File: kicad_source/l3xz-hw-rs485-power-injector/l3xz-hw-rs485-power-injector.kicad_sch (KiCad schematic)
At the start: 14 parts, among them J1 PowerPole, J2 Conn_01x02, J3 Conn_01x03, J4 SM04B-GHS-TB, J5 EH_S4B-EH, J6 EH_S4B-EH

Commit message: updated pcb
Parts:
- D1: footprint (none) -> LED_SMD:LED_0603_1608Metric
- H1, H2, H3, H4: footprint (none) -> MountingHole:MountingHole_3.2mm_M3_DIN965_Pad; now left out of the parts list
- R1: footprint (none) -> Resistor_SMD:R_0603_1608Metric
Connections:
- no-connect marks 4 -> 5
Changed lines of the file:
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@@
   )
   (no_connect (at 76.2 194.31))
+  (no_connect (at 57.15 109.22))
   (no_connect (at 50.8 194.31))
   (no_connect (at 25.4 194.31))
@@
   )
   (symbol (lib_id "Mechanical:MountingHole_Pad") (at 25.4 191.77 0) (unit 1)
-    (in_bom yes) (on_board yes) (fields_autoplaced)
+    (in_bom no) (on_board yes) (fields_autoplaced)
     (property "Reference" "H1" (id 0) (at 27.94 189.2299 0)
       (effects (font (size 1.27 1.27)) (justify left))
@@
       (effects (font (size 1.27 1.27)) (justify left))
     )
-    (property "Footprint" "" (id 2) (at 25.4 191.77 0)
+    (property "Footprint" "MountingHole:MountingHole_3.2mm_M3_DIN965_Pad" (id 2) (at 25.4 191.77 0)
       (effects (font (size 1.27 1.27)) hide)
     )
@@
   )
   (symbol (lib_id "Mechanical:MountingHole_Pad") (at 76.2 191.77 0) (unit 1)
-    (in_bom yes) (on_board yes) (fields_autoplaced)
+    (in_bom no) (on_board yes) (fields_autoplaced)
     (property "Reference" "H3" (id 0) (at 78.74 189.2299 0)
       (effects (font (size 1.27 1.27)) (justify left))
@@
       (effects (font (size 1.27 1.27)) (justify left))
     )
-    (property "Footprint" "" (id 2) (at 76.2 191.77 0)
+    (property "Footprint" "MountingHole:MountingHole_3.2mm_M3_DIN965_Pad" (id 2) (at 76.2 191.77 0)
       (effects (font (size 1.27 1.27)) hide)
     )
@@
   )
   (symbol (lib_id "Mechanical:MountingHole_Pad") (at 101.6 191.77 0) (unit 1)
-    (in_bom yes) (on_board yes) (fields_autoplaced)
+    (in_bom no) (on_board yes) (fields_autoplaced)
     (property "Reference" "H4" (id 0) (at 104.14 189.2299 0)
       (effects (font (size 1.27 1.27)) (justify left))
@@
       (effects (font (size 1.27 1.27)) (justify left))
     )
-    (property "Footprint" "" (id 2) (at 101.6 191.77 0)
+    (property "Footprint" "MountingHole:MountingHole_3.2mm_M3_DIN965_Pad" (id 2) (at 101.6 191.77 0)
       (effects (font (size 1.27 1.27)) hide)
     )
@@
     (property "Reference" "D1" (id 0) (at 118.0465 60.96 0))
     (property "Value" "LED green" (id 1) (at 118.0465 63.5 0))
-    (property "Footprint" "" (id 2) (at 118.11 67.31 90)
+    (property "Footprint" "LED_SMD:LED_0603_1608Metric" (id 2) (at 118.11 67.31 90)
       (effects (font (size 1.27 1.27)) hide)
     )
@@
   )
   (symbol (lib_id "Mechanical:MountingHole_Pad") (at 50.8 191.77 0) (unit 1)
-    (in_bom yes) (on_board yes) (fields_autoplaced)
+    (in_bom no) (on_board yes) (fields_autoplaced)
     (property "Reference" "H2" (id 0) (at 53.34 189.2299 0)
       (effects (font (size 1.27 1.27)) (justify left))
@@
       (effects (font (size 1.27 1.27)) (justify left))
     )
-    (property "Footprint" "" (id 2) (at 50.8 191.77 0)
+    (property "Footprint" "MountingHole:MountingHole_3.2mm_M3_DIN965_Pad" (id 2) (at 50.8 191.77 0)
       (effects (font (size 1.27 1.27)) hide)
     )
@@
     (property "Reference" "R1" (id 0) (at 107.95 60.96 90))
     (property "Value" "10k" (id 1) (at 107.95 63.5 90))
-    (property "Footprint" "" (id 2) (at 107.95 67.31 0)
+    (property "Footprint" "Resistor_SMD:R_0603_1608Metric" (id 2) (at 107.95 67.31 0)
       (effects (font (size 1.27 1.27)) hide)
     )
@@
     )
     (path "/a191106d-6f54-4859-9ae7-7e90c19ff902"
-      (reference "D1") (unit 1) (value "LED green") (footprint "")
+      (reference "D1") (unit 1) (value "LED green") (footprint "LED_SMD:LED_0603_1608Metric")
     )
     (path "/0f7a0782-5c93-425e-9bb2-af249e5413b1"
-      (reference "H1") (unit 1) (value "MountingHole_Pad") (footprint "")
+      (reference "H1") (unit 1) (value "MountingHole_Pad") (footprint "MountingHole:MountingHole_3.2mm_M3_DIN965_Pad")
     )
     (path "/a24d063b-8999-4513-be31-467144dda607"
-      (reference "H2") (unit 1) (value "MountingHole_Pad") (footprint "")
+      (reference "H2") (unit 1) (value "MountingHole_Pad") (footprint "MountingHole:MountingHole_3.2mm_M3_DIN965_Pad")
     )
     (path "/1a89f90c-ae34-4a19-bdb2-498363cb9261"
-      (reference "H3") (unit 1) (value "MountingHole_Pad") (footprint "")
+      (reference "H3") (unit 1) (value "MountingHole_Pad") (footprint "MountingHole:MountingHole_3.2mm_M3_DIN965_Pad")
     )
     (path "/549e08a5-626b-4ce1-b4f2-0dc3abb4166a"
-      (reference "H4") (unit 1) (value "MountingHole_Pad") (footprint "")
+      (reference "H4") (unit 1) (value "MountingHole_Pad") (footprint "MountingHole:MountingHole_3.2mm_M3_DIN965_Pad")
     )
     (path "/9cff36d3-3837-47cf-8e03-52d1bf5a2a97"
@@
     )
     (path "/d10997a4-c66c-4c0c-b0e2-7abe2be8864b"
-      (reference "R1") (unit 1) (value "10k") (footprint "")
-    )
-  )
+      (reference "R1") (unit 1) (value "10k") (footprint "Resistor_SMD:R_0603_1608Metric")
+    )
+  )

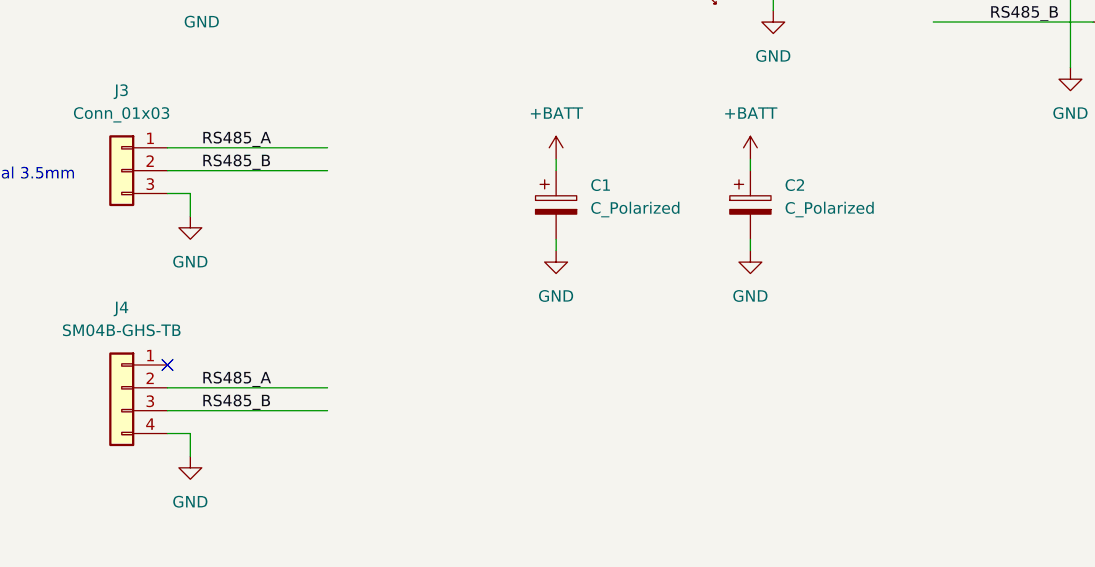
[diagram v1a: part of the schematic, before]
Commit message: added resistor to connect JST GH connector to +BATT
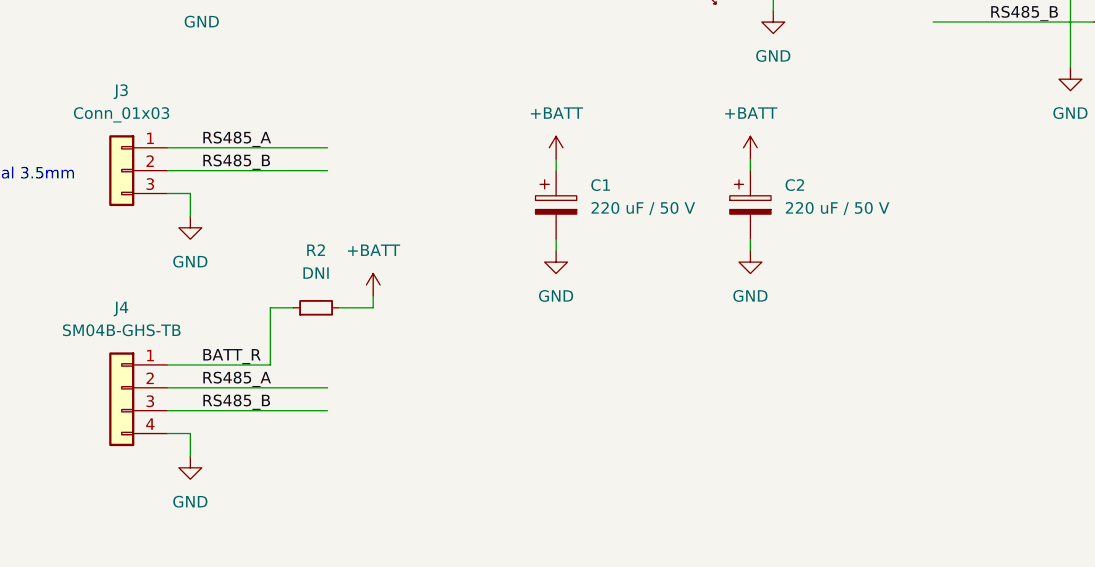
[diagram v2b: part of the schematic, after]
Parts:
- added R2: DNI, Resistor_SMD:R_0603_1608Metric, symbol Device:R_Small
- C1, C2: value C_Polarized -> 220 uF / 50 V
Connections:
- net +BATT: now also R2.2
- net BATT_R: now reaches J4.1 (Pin_1)
- net BATT_R: now also R2.1
- no-connect marks 5 -> 4
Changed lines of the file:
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@@
   (title_block
     (title "l3xz-hw-rs485-power-injector")
-    (date "2023-01-07")
+    (date "2023-01-21")
     (rev "0.1")
     (company "107-systems")
   )
   (no_connect (at 76.2 194.31))
-  (no_connect (at 57.15 109.22))
   (no_connect (at 50.8 194.31))
   (no_connect (at 25.4 194.31))
@@
     (stroke (width 0) (type default) (color 0 0 0 0))
   )
+  (wire (pts (xy 68.58 102.87) (xy 68.58 109.22))
+    (stroke (width 0) (type default) (color 0 0 0 0))
+  )
   (wire (pts (xy 57.15 114.3) (xy 74.93 114.3))
     (stroke (width 0) (type default) (color 0 0 0 0))
   )
+  (wire (pts (xy 71.12 102.87) (xy 68.58 102.87))
+    (stroke (width 0) (type default) (color 0 0 0 0))
+  )
   (wire (pts (xy 60.96 63.5) (xy 60.96 66.04))
     (stroke (width 0) (type default) (color 0 0 0 0))
@@
     (stroke (width 0) (type default) (color 0 0 0 0))
   )
+  (wire (pts (xy 76.2 102.87) (xy 80.01 102.87))
+    (stroke (width 0) (type default) (color 0 0 0 0))
+  )
   (wire (pts (xy 57.15 87.63) (xy 74.93 87.63))
     (stroke (width 0) (type default) (color 0 0 0 0))
@@
     (stroke (width 0) (type default) (color 0 0 0 0))
   )
+  (wire (pts (xy 80.01 102.87) (xy 80.01 101.6))
+    (stroke (width 0) (type default) (color 0 0 0 0))
+  )
   (wire (pts (xy 121.92 86.36) (xy 121.92 87.63))
     (stroke (width 0) (type default) (color 0 0 0 0))
@@
   )
   (wire (pts (xy 157.48 63.5) (xy 157.48 76.2))
+    (stroke (width 0) (type default) (color 0 0 0 0))
+  )
+  (wire (pts (xy 68.58 109.22) (xy 57.15 109.22))
     (stroke (width 0) (type default) (color 0 0 0 0))
   )
@@
   (label "RS485_A" (at 156.21 68.58 180)
     (effects (font (size 1.27 1.27)) (justify right bottom))
+  )
+  (label "BATT_R" (at 60.96 109.22 0)
+    (effects (font (size 1.27 1.27)) (justify left bottom))
   )
   (label "RS485_A" (at 60.96 85.09 0)
@@
     (pin "1")
   )
+  (symbol (lib_id "power:+BATT") (at 80.01 101.6 0) (unit 1)
+    (in_bom yes) (on_board yes) (fields_autoplaced)
+    (property "Reference" "#PWR017" (id 0) (at 80.01 105.41 0)
+      (effects (font (size 1.27 1.27)) hide)
+    )
+    (property "Value" "+BATT" (id 1) (at 80.01 96.52 0))
+    (property "Footprint" "" (id 2) (at 80.01 101.6 0)
+      (effects (font (size 1.27 1.27)) hide)
+    )
+    (property "Datasheet" "" (id 3) (at 80.01 101.6 0)
+      (effects (font (size 1.27 1.27)) hide)
+    )
+    (pin "1")
+  )
   (symbol (lib_id "Mechanical:MountingHole_Pad") (at 76.2 191.77 0) (unit 1)
     (in_bom no) (on_board yes) (fields_autoplaced)
@@
       (effects (font (size 1.27 1.27)) (justify left))
     )
-    (property "Value" "C_Polarized" (id 1) (at 125.73 91.8209 0)
+    (property "Value" "220 uF / 50 V" (id 1) (at 125.73 91.8209 0)
       (effects (font (size 1.27 1.27)) (justify left))
     )
@@
       (effects (font (size 1.27 1.27)) (justify left))
     )
-    (property "Value" "C_Polarized" (id 1) (at 104.14 91.8209 0)
+    (property "Value" "220 uF / 50 V" (id 1) (at 104.14 91.8209 0)
       (effects (font (size 1.27 1.27)) (justify left))
     )
@@
     (pin "1")
   )
+  (symbol (lib_id "Device:R_Small") (at 73.66 102.87 90) (unit 1)
+    (in_bom yes) (on_board yes) (fields_autoplaced)
+    (property "Reference" "R2" (id 0) (at 73.66 96.52 90))
+    (property "Value" "DNI" (id 1) (at 73.66 99.06 90))
+    (property "Footprint" "Resistor_SMD:R_0603_1608Metric" (id 2) (at 73.66 102.87 0)
+      (effects (font (size 1.27 1.27)) hide)
+    )
+    (property "Datasheet" "~" (id 3) (at 73.66 102.87 0)
+      (effects (font (size 1.27 1.27)) hide)
+    )
+    (pin "1")
+    (pin "2")
+  )
   (sheet_instances
     (path "/" (page "1"))
@@
       (reference "#PWR016") (unit 1) (value "GND") (footprint "")
     )
+    (path "/11c1ce21-067e-4535-a9d6-af1642672693"
+      (reference "#PWR017") (unit 1) (value "+BATT") (footprint "")
+    )
     (path "/6a72edad-3f19-4c57-a92a-dc01de1e97e0"
-      (reference "C1") (unit 1) (value "C_Polarized") (footprint "Capacitor_SMD:CP_Elec_10x14.3")
+      (reference "C1") (unit 1) (value "220 uF / 50 V") (footprint "Capacitor_SMD:CP_Elec_10x14.3")
     )
     (path "/32589f51-a0e1-4d83-8926-fda75fe5d2da"
-      (reference "C2") (unit 1) (value "C_Polarized") (footprint "Capacitor_SMD:CP_Elec_10x14.3")
+      (reference "C2") (unit 1) (value "220 uF / 50 V") (footprint "Capacitor_SMD:CP_Elec_10x14.3")
     )
     (path "/a191106d-6f54-4859-9ae7-7e90c19ff902"
@@
       (reference "R1") (unit 1) (value "10k") (footprint "Resistor_SMD:R_0603_1608Metric")
     )
-  )
+    (path "/fc5500b2-c6f1-402d-8b60-b8c2e44f7499"
+      (reference "R2") (unit 1) (value "DNI") (footprint "Resistor_SMD:R_0603_1608Metric")
+    )
+  )

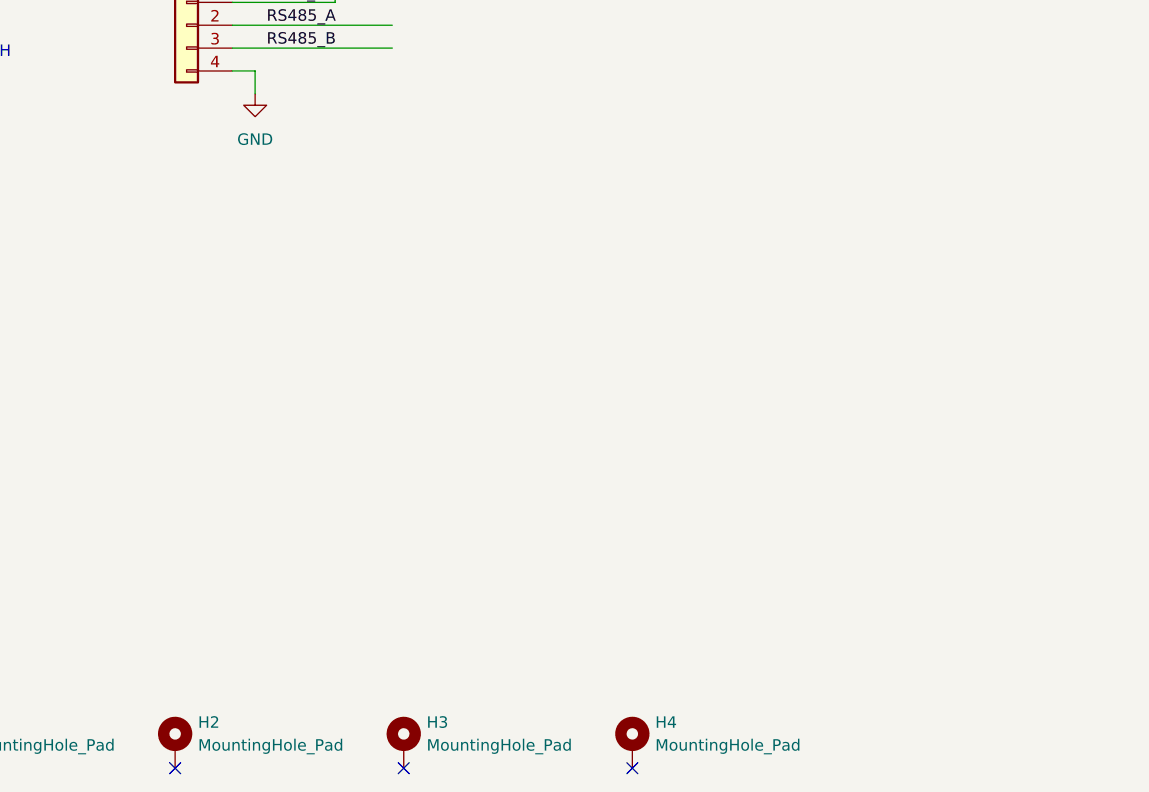
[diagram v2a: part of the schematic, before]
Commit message: added RS-485 transceiver and status LED
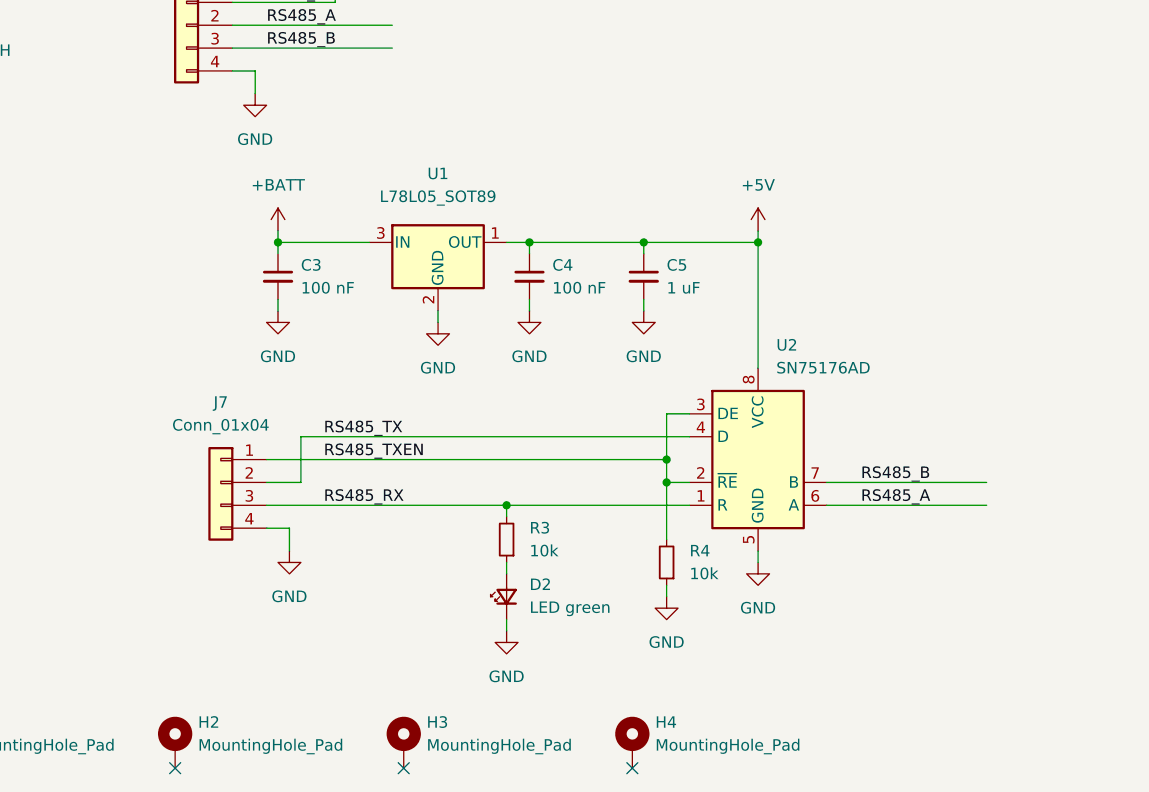
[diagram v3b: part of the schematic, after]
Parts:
- added C3, C4: 100 nF, Capacitor_SMD:C_0603_1608Metric, symbol Device:C_Small
- added C5: 1 uF, Capacitor_SMD:C_0603_1608Metric, symbol Device:C_Small
- added D2: LED green, LED_SMD:LED_0603_1608Metric, symbol Device:LED_Small
- added J7: Conn_01x04, Connector_PinHeader_2.54mm:PinHeader_1x04_P2.54mm_Vertical, symbol Connector_Generic:Conn_01x04
- added R3, R4: 10k, Resistor_SMD:R_0603_1608Metric, symbol Device:R_Small
- added U1: L78L05_SOT89, Package_TO_SOT_SMD:SOT-89-3, symbol Regulator_Linear:L78L05_SOT89
- added U2: SN75176AD, Package_SO:SOIC-8_3.9x4.9mm_P1.27mm, symbol Interface_UART:SN75176AD
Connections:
- net +BATT: now also C3.1, U1.3 (IN)
- net GND: now also C3.2, C4.2, C5.2, D2.1 (K), J7.4 (Pin_4), R4.1, U1.2 (GND), U2.5 (GND)
- net RS485_A: now also U2.6 (A)
- net RS485_B: now also U2.7 (B)
- new net: D2.2 (A), R3.1
- new net +5V: C4.1, C5.1, U1.1 (OUT), U2.8 (VCC)
- new net RS485_RX: J7.3 (Pin_3), R3.2, U2.1 (R)
- new net RS485_TX: J7.2 (Pin_2), U2.4 (D)
- new net RS485_TXEN: J7.1 (Pin_1), R4.2, U2.2 (~{RE}), U2.3 (DE)

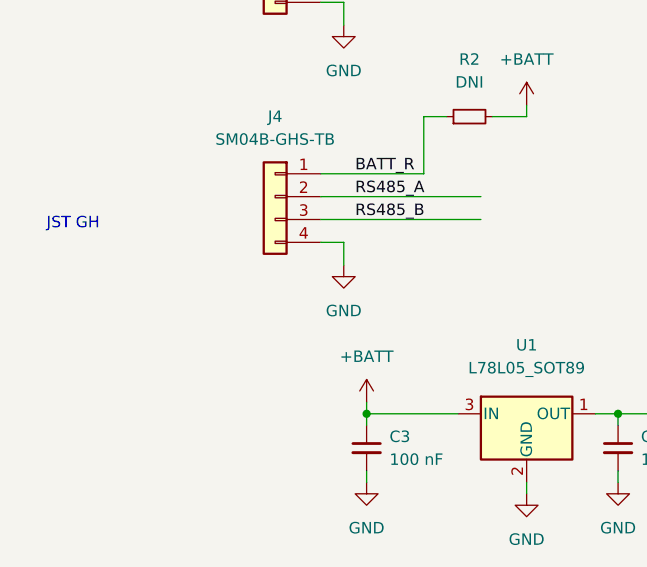
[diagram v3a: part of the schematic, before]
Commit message: added mounting pad on JST GH connector
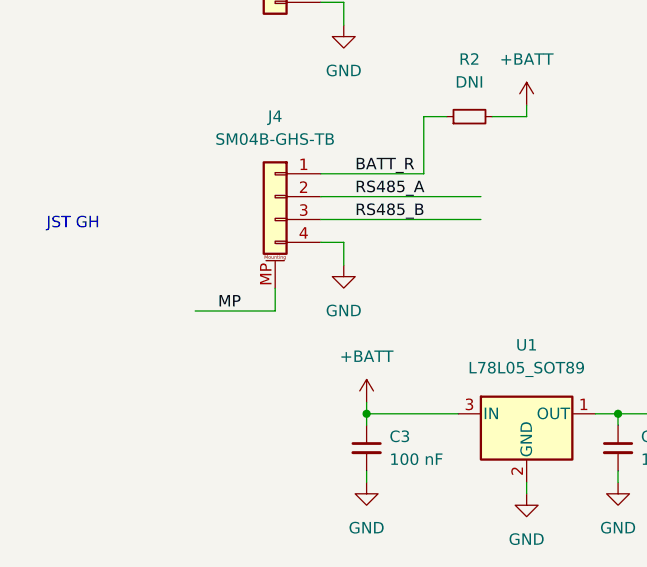
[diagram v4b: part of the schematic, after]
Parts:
- J4: symbol Connector_Generic:Conn_01x04 -> Connector_Generic_MountingPin:Conn_01x04_MountingPin
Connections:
- new net MP: J4.MP (MountPin)
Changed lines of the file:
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@@
+    (stroke (width 0) (type default) (color 0 0 0 0))
+  )
+  (wire (pts (xy 52.07 124.46) (xy 52.07 121.92))
     (stroke (width 0) (type default) (color 0 0 0 0))
   )
@@
   )
   (wire (pts (xy 100.33 86.36) (xy 100.33 87.63))
+    (stroke (width 0) (type default) (color 0 0 0 0))
+  )
+  (wire (pts (xy 43.18 124.46) (xy 52.07 124.46))
     (stroke (width 0) (type default) (color 0 0 0 0))
   )
@@
   )
   (label "RS485_B" (at 60.96 114.3 0)
+    (effects (font (size 1.27 1.27)) (justify left bottom))
+  )
+  (label "MP" (at 45.72 124.46 0)
     (effects (font (size 1.27 1.27)) (justify left bottom))
   )
@@
     (pin "1")
   )
-  (symbol (lib_id "Connector_Generic:Conn_01x04") (at 52.07 111.76 0) (mirror y) (unit 1)
+  (symbol (lib_id "Connector_Generic_MountingPin:Conn_01x04_MountingPin") (at 52.07 111.76 0) (mirror y) (unit 1)
     (in_bom yes) (on_board yes) (fields_autoplaced)
     (property "Reference" "J4" (id 0) (at 52.07 102.87 0))
@@
     (pin "3")
     (pin "4")
+    (pin "MP")
   )
   (symbol (lib_id "Connector_Generic:Conn_01x04") (at 165.1 66.04 0) (unit 1)
